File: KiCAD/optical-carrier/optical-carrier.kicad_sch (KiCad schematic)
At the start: 9 parts, among them J1 Conn_02x08_Odd_Even

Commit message: branch for V2
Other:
- note added: "REV 2 WORK IN PROGRESS"
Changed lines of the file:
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@@
 	(generator_version "9.0")
 	(paper "A4")
+	(text "REV 2 WORK IN PROGRESS"
+		(exclude_from_sim no)
+		(at 242.062 174.244 0)
+		(effects
+			(font
+				(size 2.54 2.54)
+			)
+		)
+	)
 	(wire
 		(pts

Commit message: working on v2 layout
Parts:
- added D1, D5: LED_GABR, my_LED:Marubeni, symbol Device:LED_GABR
- added JP1: Jumper_3_Bridged12, Connector_PinHeader_2.54mm:PinHeader_1x03_P2.54mm_Vertical, symbol Jumper:Jumper_3_Bridged12
- added TH1: Thermistor, Resistor_SMD:R_0603_1608Metric_Pad0.98x0.95mm_HandSolder, symbol Device:Thermistor
- renumbered D3 to D2, D1 to D3, D2 to D6
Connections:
- net at D3.2 (A): now also D2.2 (A), D6.2 (A), J1.10 (Pin_10), J1.8 (Pin_8), D1.2 (A), D5.2 (A); no longer J1.1 (Pin_1)
- net LED1: now reaches D2.1 (K)
- net LED1: now also J1.1 (Pin_1); no longer J1.11 (Pin_11)
- net LED7: now reaches J1.13 (Pin_13)
- net LED7: now also D5.1 (GK)
- net at J1.14 (Pin_14): now also TH1.2
- net LED8: now reaches J1.15 (Pin_15)
- net LED8: now also JP1.2 (C)
- net LED2: now reaches D3.1 (K), J1.3 (Pin_3)
- net LED3: now reaches J1.5 (Pin_5)
- net LED3: now also D1.4 (RK); no longer D6.2 (A)
- net at J1.6 (Pin_6): now also TH1.1
- net at D6.1 (K): now also JP1.3 (B); no longer J1.7 (Pin_7)
- net LED5: now reaches J1.9 (Pin_9)
- net LED5: now also D1.3 (BK); no longer D2.2 (A)
- new net: D5.3 (BK), JP1.1 (A)
- new net LED4: D1.1 (GK), J1.7 (Pin_7)
- new net LED6: D5.4 (RK), J1.11 (Pin_11)
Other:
- moved on the sheet: D2, D3, D6, H1, H2, H3, H4

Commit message: routing done?
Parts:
- renumbered D5 to D1, D3 to D2, D2 to D3, D6 to D4, D1 to D5, D4 to D6
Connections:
- net LED1: now also D1.1 (GK); no longer D3.1 (K)
- net LED3: now also D1.4 (RK); no longer D5.4 (RK)
- net LED4: now also JP1.2 (C); no longer D5.1 (GK)
- net LED5: now also D5.1 (GK); no longer D5.3 (BK)
- net LED6: now also D3.1 (K); no longer D1.4 (RK)
- net LED7: now also D5.4 (RK); no longer D1.1 (GK)
- net LED8: now also D5.3 (BK); no longer JP1.2 (C)
- net at J1.14 (Pin_14), TH1.2: now also D6.2 (A), J1.4 (Pin_4)
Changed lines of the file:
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@@
+	)
+	(junction
+		(at 140.97 77.47)
+		(diameter 0)
+		(color 0 0 0 0)
+	)
+	(junction
+		(at 140.97 85.09)
+		(diameter 0)
+		(color 0 0 0 0)
 	)
 	(junction
@@
 	(wire
 		(pts
-			(xy 133.35 85.09) (xy 167.64 85.09)
+			(xy 133.35 85.09) (xy 140.97 85.09)
 		)
 		(stroke
@@
 	(wire
 		(pts
+			(xy 140.97 77.47) (xy 140.97 85.09)
+		)
+		(stroke
+			(width 0)
+			(type default)
+		)
+	)
+	(wire
+		(pts
 			(xy 133.35 72.39) (xy 140.97 72.39)
 		)
@@
 		(pts
 			(xy 151.13 134.62) (xy 173.99 134.62)
+		)
+		(stroke
+			(width 0)
+			(type default)
+		)
+	)
+	(wire
+		(pts
+			(xy 140.97 85.09) (xy 167.64 85.09)
 		)
 		(stroke
@@
 		)
 	)
-	(label "LED6"
+	(label "LED3"
 		(at 153.67 93.98 0)
 		(effects
@@
 		)
 	)
-	(label "LED1"
+	(label "LED6"
 		(at 86.36 120.65 0)
 		(effects
@@
 		)
 	)
-	(label "LED5"
+	(label "LED8"
 		(at 91.44 99.06 0)
 		(effects
@@
 		)
 	)
-	(label "LED3"
+	(label "LED7"
 		(at 91.44 93.98 0)
 		(effects
@@
 		)
 	)
-	(label "LED4"
+	(label "LED5"
 		(at 91.44 96.52 0)
 		(effects
@@
 		)
 	)
-	(label "LED7"
+	(label "LED1"
 		(at 153.67 96.52 0)
 		(effects
@@
 		)
 	)
-	(label "LED8"
+	(label "LED4"
 		(at 191.77 96.52 0)
 		(effects
@@
 		(dnp no)
 		(fields_autoplaced yes)
-		(property "Reference" "D5"
+		(property "Reference" "D1"
 			(at 160.02 106.6799 90)
 			(effects
@@
 			(project "optical-carrier"
 				(path "/d8677e2d-f25e-4f3a-9cba-3944c56fbd40"
-					(reference "D5")
+					(reference "D1")
 					(unit 1)
 				)
@@
 		(dnp no)
 		(fields_autoplaced yes)
-		(property "Reference" "D1"
+		(property "Reference" "D5"
 			(at 93.98 106.6799 90)
 			(effects
@@
 			(project ""
 				(path "/d8677e2d-f25e-4f3a-9cba-3944c56fbd40"
-					(reference "D1")
+					(reference "D5")
 					(unit 1)
 				)
@@
 		(dnp no)
 		(fields_autoplaced yes)
-		(property "Reference" "D4"
+		(property "Reference" "D6"
 			(at 152.4 72.7074 90)
 			(effects
@@
 			(project ""
 				(path "/d8677e2d-f25e-4f3a-9cba-3944c56fbd40"
-					(reference "D4")
+					(reference "D6")
 					(unit 1)
 				)
@@
 		(on_board yes)
 		(dnp no)
-		(property "Reference" "D6"
+		(property "Reference" "D4"
 			(at 154.94 125.984 90)
 			(effects
@@
 			(project "optical-carrier"
 				(path "/d8677e2d-f25e-4f3a-9cba-3944c56fbd40"
-					(reference "D6")
+					(reference "D4")
 					(unit 1)
 				)
@@
 		(on_board yes)
 		(dnp no)
-		(property "Reference" "D3"
+		(property "Reference" "D2"
 			(at 122.936 125.984 90)
 			(effects
@@
 			(project ""
 				(path "/d8677e2d-f25e-4f3a-9cba-3944c56fbd40"
-					(reference "D3")
+					(reference "D2")
 					(unit 1)
 				)
@@
 		(on_board yes)
 		(dnp no)
-		(property "Reference" "D2"
+		(property "Reference" "D3"
 			(at 88.392 126.746 90)
 			(effects
@@
 			(project "optical-carrier"
 				(path "/d8677e2d-f25e-4f3a-9cba-3944c56fbd40"
-					(reference "D2")
+					(reference "D3")
 					(unit 1)
 				)

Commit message: update schem PDF, readmes
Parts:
- H1, H2, H3, H4: footprint (none) -> MountingHole:MountingHole_4.3mm_M4_DIN965
- JP1: now not fitted
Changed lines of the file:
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@@
 			)
 		)
-		(property "Footprint" ""
+		(property "Footprint" "MountingHole:MountingHole_4.3mm_M4_DIN965"
 			(at 54.61 170.18 0)
 			(effects
@@
 			)
 		)
-		(property "Footprint" ""
+		(property "Footprint" "MountingHole:MountingHole_4.3mm_M4_DIN965"
 			(at 54.61 175.26 0)
 			(effects
@@
 			)
 		)
-		(property "Footprint" ""
+		(property "Footprint" "MountingHole:MountingHole_4.3mm_M4_DIN965"
 			(at 54.61 160.02 0)
 			(effects
@@
 		(in_bom no)
 		(on_board yes)
-		(dnp no)
+		(dnp yes)
 		(property "Reference" "JP1"
 			(at 191.77 110.49 0)
@@
 			)
 		)
-		(property "Footprint" ""
+		(property "Footprint" "MountingHole:MountingHole_4.3mm_M4_DIN965"
 			(at 54.61 165.1 0)
 			(effects

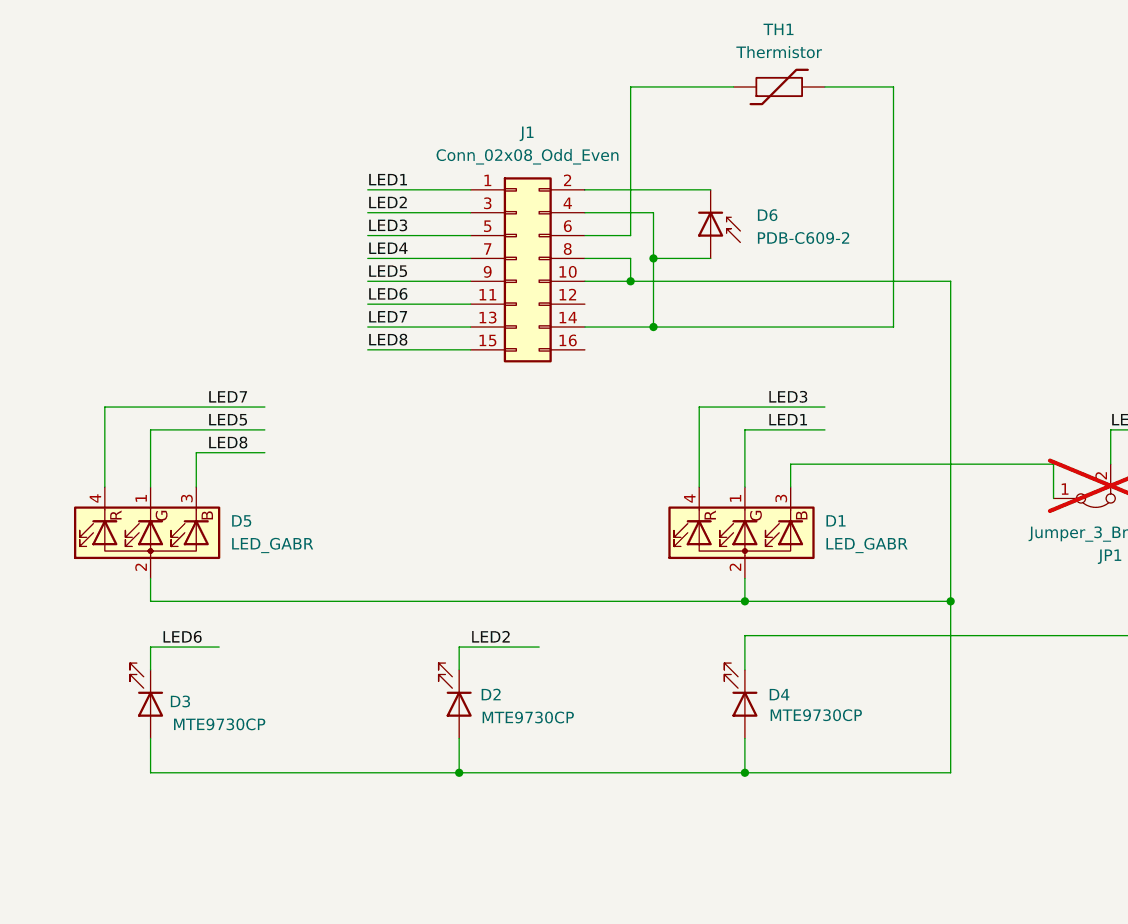
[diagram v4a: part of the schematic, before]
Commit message: Add op-amp buffer on temp sensor
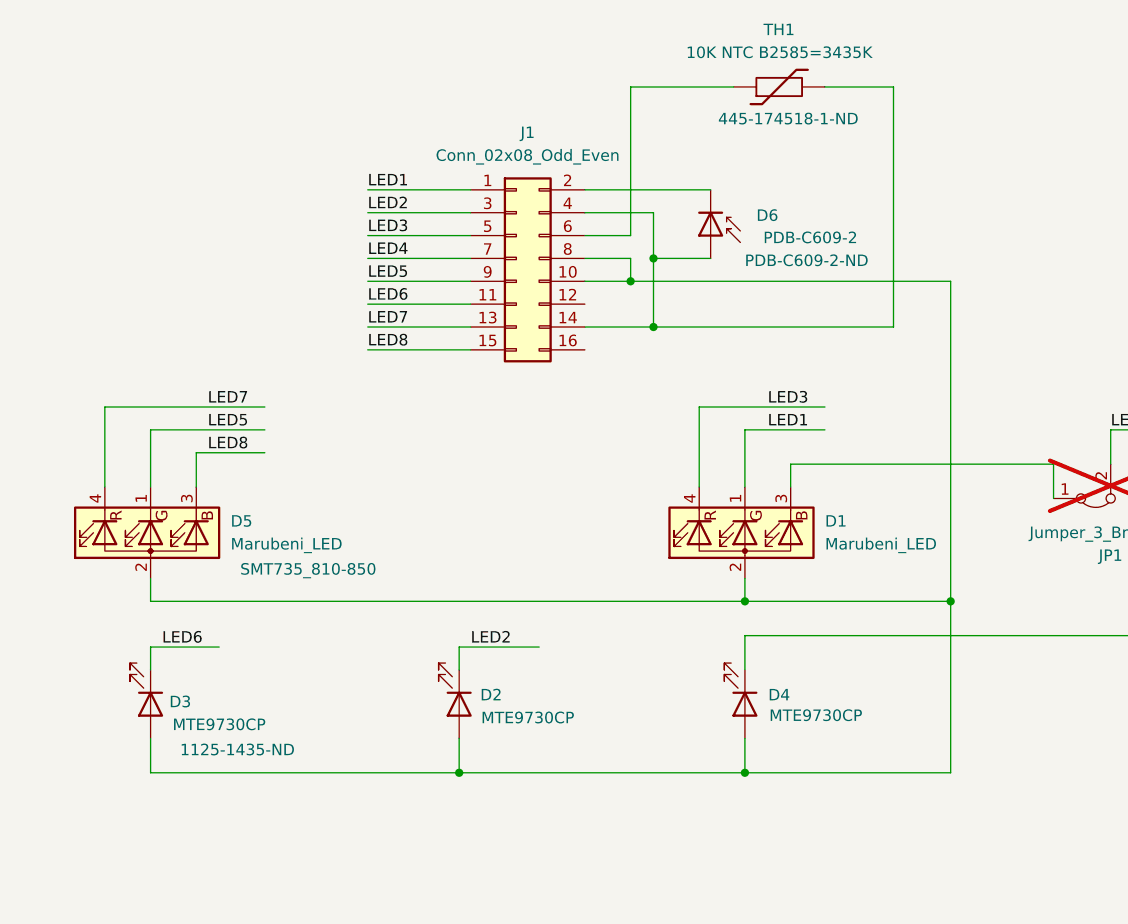
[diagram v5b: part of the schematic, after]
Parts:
- D1, D5: value LED_GABR -> Marubeni_LED; MfgNo (none) -> SMT735_810-850
- D2, D4: CatNo (none) -> 1125-1435-ND; MfgNo (none) -> MTE9730CP
- D3: CatNo (none) -> 1125-1435-ND; DigikeyNumber 1125-1435-ND -> (none); ManufacturerNumber MTE9730CP -> (none); MfgNo (none) -> MTE9730CP
- D6: CatNo (none) -> PDB-C609-2-ND; DigikeyNumber PDB-C609-2-ND -> (none); MfgNo (none) -> PDB-C609-2
- TH1: value Thermistor -> 10K NTC B2585=3435K; CatNo (none) -> 445-174518-1-ND; MfgNo (none) -> NTCG163JX103DT1S
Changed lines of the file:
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@@
 			)
 		)
-		(property "Value" "LED_GABR"
+		(property "Value" "Marubeni_LED"
 			(at 160.02 109.2199 90)
 			(effects
@@
 			)
 		)
-		(property "Datasheet" "~"
+		(property "Datasheet" "https://tech-led.com/wp-content/uploads/2019/04/SMT735_810_850-1.pdf"
 			(at 152.4 107.95 0)
 			(effects
@@
 		(property "Description" "RGB LED, green/anode/blue/red"
 			(at 151.13 107.95 0)
+			(effects
+				(font
+					(size 1.27 1.27)
+				)
+				(hide yes)
+			)
+		)
+		(property "MfgNo" "SMT735_810-850"
+			(at 151.13 107.95 90)
 			(effects
 				(font
@@
 		(on_board yes)
 		(dnp no)
-		(fields_autoplaced yes)
 		(property "Reference" "D5"
 			(at 93.98 106.6799 90)
@@
 			)
 		)
-		(property "Value" "LED_GABR"
+		(property "Value" "Marubeni_LED"
 			(at 93.98 109.2199 90)
 			(effects
@@
 			)
 		)
-		(property "Datasheet" "~"
+		(property "Datasheet" "https://tech-led.com/wp-content/uploads/2019/04/SMT735_810_850-1.pdf"
 			(at 86.36 107.95 0)
 			(effects
@@
 				)
 				(hide yes)
+			)
+		)
+		(property "MfgNo" "SMT735_810-850"
+			(at 102.616 112.014 90)
+			(effects
+				(font
+					(size 1.27 1.27)
+				)
 			)
 		)
@@
 		(on_board yes)
 		(dnp no)
-		(fields_autoplaced yes)
 		(property "Reference" "D6"
 			(at 152.4 72.7074 90)
@@
 		)
 		(property "Value" "PDB-C609-2"
-			(at 152.4 75.2474 90)
+			(at 153.162 75.184 90)
 			(effects
 				(font
@@
 			)
 		)
-		(property "DigikeyNumber" "PDB-C609-2-ND"
+		(property "CatNo" "PDB-C609-2-ND"
+			(at 157.988 77.724 90)
+			(effects
+				(font
+					(size 1.27 1.27)
+				)
+			)
+		)
+		(property "MfgNo" "PDB-C609-2"
 			(at 147.32 74.93 90)
 			(effects
@@
 		(on_board yes)
 		(dnp no)
-		(fields_autoplaced yes)
 		(property "Reference" "TH1"
 			(at 154.94 52.07 90)
@@
 			)
 		)
-		(property "Value" "Thermistor"
+		(property "Value" "10K NTC B2585=3435K"
 			(at 154.94 54.61 90)
 			(effects
@@
 			)
 		)
-		(property "Datasheet" "~"
+		(property "Datasheet" "https://product.tdk.com/en/search/sensor/ntc/chip-ntc-thermistor/info?part_no=NTCG163JX103DT1S"
 			(at 154.94 58.42 0)
 			(effects
@@
 		(property "Description" "Temperature dependent resistor"
 			(at 154.94 58.42 0)
+			(effects
+				(font
+					(size 1.27 1.27)
+				)
+				(hide yes)
+			)
+		)
+		(property "CatNo" "445-174518-1-ND"
+			(at 155.956 61.976 90)
+			(effects
+				(font
+					(size 1.27 1.27)
+				)
+			)
+		)
+		(property "MfgNo" "NTCG163JX103DT1S"
+			(at 154.94 58.42 90)
 			(effects
 				(font
@@
 			)
 		)
-		(property "Datasheet" "~"
+		(property "Datasheet" "https://specs.marktechopto.com/pdf/products/datasheet/MTE9730CP.pdf"
 			(at 151.13 127 0)
 			(effects
@@
 		(property "ManufacturerNumber" "MTE9730CP"
 			(at 151.13 127 0)
+			(effects
+				(font
+					(size 1.27 1.27)
+				)
+				(hide yes)
+			)
+		)
+		(property "CatNo" "1125-1435-ND"
+			(at 151.13 127 90)
+			(effects
+				(font
+					(size 1.27 1.27)
+				)
+				(hide yes)
+			)
+		)
+		(property "MfgNo" "MTE9730CP"
+			(at 151.13 127 90)
 			(effects
 				(font
@@
 			)
 		)
-		(property "Datasheet" "~"
+		(property "Datasheet" "https://specs.marktechopto.com/pdf/products/datasheet/MTE9730CP.pdf"
 			(at 119.38 127 0)
 			(effects
@@
 		(property "ManufacturerNumber" "MTE9730CP"
 			(at 119.38 127 0)
+			(effects
+				(font
+					(size 1.27 1.27)
+				)
+				(hide yes)
+			)
+		)
+		(property "CatNo" "1125-1435-ND"
+			(at 119.38 127 90)
+			(effects
+				(font
+					(size 1.27 1.27)
+				)
+				(hide yes)
+			)
+		)
+		(property "MfgNo" "MTE9730CP"
+			(at 119.38 127 90)
 			(effects
 				(font
@@
 			)
 		)
-		(property "Datasheet" "~"
+		(property "Datasheet" "https://specs.marktechopto.com/pdf/products/datasheet/MTE9730CP.pdf"
 			(at 85.09 127 0)
 			(effects
@@
 			)
 		)
-		(property "DigikeyNumber" "1125-1435-ND"
+		(property "CatNo" "1125-1435-ND"
+			(at 94.742 132.08 90)
+			(effects
+				(font
+					(size 1.27 1.27)
+				)
+			)
+		)
+		(property "MfgNo" "MTE9730CP"
 			(at 85.09 127 0)
 			(effects
-				(font
-					(size 1.27 1.27)
-				)
-				(hide yes)
-			)
-		)
-		(property "ManufacturerNumber" "MTE9730CP"
-			(at 85.09 127 0)
-			(effects

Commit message: Rev 2.0 for review
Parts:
- D1, D5, H1, H2, H3, H4: now not fitted
- D2, D4: DigikeyNumber 1125-1435-ND -> (none); ManufacturerNumber MTE9730CP -> (none)
- J1: CatNo (none) -> S9196-ND; MfgNo (none) -> SFH11-PBPC-D08-ST-BK
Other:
- note added: "REV 2.0 10/19/25"
- note removed: "REV 2 WORK IN PROGRESS"
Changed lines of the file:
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@@
 	(generator_version "9.0")
 	(paper "A4")
-	(text "REV 2 WORK IN PROGRESS"
+	(text "REV 2.0\n10/19/25"
 		(exclude_from_sim no)
 		(at 242.062 174.244 0)
@@
 			)
 		)
+		(property "CatNo" "S9196-ND"
+			(at 125.73 77.47 0)
+			(effects
+				(font
+					(size 1.27 1.27)
+				)
+				(hide yes)
+			)
+		)
+		(property "MfgNo" "SFH11-PBPC-D08-ST-BK"
+			(at 125.73 77.47 0)
+			(effects
+				(font
+					(size 1.27 1.27)
+				)
+				(hide yes)
+			)
+		)
 		(pin "16"
 		)
@@
 		(in_bom yes)
 		(on_board yes)
-		(dnp no)
+		(dnp yes)
 		(fields_autoplaced yes)
 		(property "Reference" "D1"
@@
 		(in_bom yes)
 		(on_board yes)
-		(dnp no)
+		(dnp yes)
 		(property "Reference" "D5"
 			(at 93.98 106.6799 90)
@@
 		(in_bom no)
 		(on_board yes)
-		(dnp no)
+		(dnp yes)
 		(fields_autoplaced yes)
 		(property "Reference" "H3"
@@
 		(in_bom no)
 		(on_board yes)
-		(dnp no)
+		(dnp yes)
 		(fields_autoplaced yes)
 		(property "Reference" "H4"
@@
 		(in_bom no)
 		(on_board yes)
-		(dnp no)
+		(dnp yes)
 		(fields_autoplaced yes)
 		(property "Reference" "H1"
@@
 			)
 		)
-		(property "DigikeyNumber" "1125-1435-ND"
+		(property "DigikeyNumber" ""
 			(at 151.13 127 0)
 			(effects
@@
 			)
 		)
-		(property "ManufacturerNumber" "MTE9730CP"
+		(property "ManufacturerNumber" ""
 			(at 151.13 127 0)
 			(effects
@@
 			)
 		)
-		(property "DigikeyNumber" "1125-1435-ND"
+		(property "DigikeyNumber" ""
 			(at 119.38 127 0)
 			(effects
@@
 			)
 		)
-		(property "ManufacturerNumber" "MTE9730CP"
+		(property "ManufacturerNumber" ""
 			(at 119.38 127 0)
 			(effects
@@
 		(in_bom no)
 		(on_board yes)
-		(dnp no)
+		(dnp yes)
 		(fields_autoplaced yes)
 		(property "Reference" "H2"

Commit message: hopefully final Rev 2
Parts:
- D1, D5: symbol Device:LED_GABR -> my_Marubeni:LED_Maru
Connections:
- net LED1: now also D1.2 (GK); no longer D1.1 (GK)
- net LED5: now also D5.2 (GK); no longer D5.1 (GK)
- net at D2.2 (A), D3.2 (A), D4.2 (A)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: now also D1.1 (A), D5.1 (A); no longer D1.2 (A), D5.2 (A)
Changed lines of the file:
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@@
 	)
 	(symbol
-		(lib_id "Device:LED_GABR")
+		(lib_id "my_Marubeni:LED_Maru")
 		(at 151.13 107.95 90)
 		(mirror x)
@@
 			)
 		)
-		(property "Datasheet" "https://tech-led.com/wp-content/uploads/2019/04/SMT735_810_850-1.pdf"
+		(property "Datasheet" "~"
 			(at 152.4 107.95 0)
 			(effects
@@
 	)
 	(symbol
-		(lib_id "Device:LED_GABR")
+		(lib_id "my_Marubeni:LED_Maru")
 		(at 85.09 107.95 90)
 		(mirror x)
@@
 			)
 		)
-		(property "Datasheet" "https://tech-led.com/wp-content/uploads/2019/04/SMT735_810_850-1.pdf"
+		(property "Datasheet" "~"
 			(at 86.36 107.95 0)
 			(effects
